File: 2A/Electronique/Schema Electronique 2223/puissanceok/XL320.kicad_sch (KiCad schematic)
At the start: 9 parts, among them J17 Conn_01x03, U4 74LVC2G241

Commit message: pcb puissance update
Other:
- moved on the sheet: C15, U4C
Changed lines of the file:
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@@
   (junction (at 156.6362 74.168) (diameter 0) (color 0 0 0 0)
   )
-  (junction (at 181.61 97.79) (diameter 0) (color 0 0 0 0)
+  (junction (at 144.018 77.724) (diameter 0) (color 0 0 0 0)
   )
   (junction (at 171.196 82.296) (diameter 0) (color 0 0 0 0)
@@
   (junction (at 163.8824 76.708) (diameter 0) (color 0 0 0 0)
   )
-  (junction (at 181.61 118.11) (diameter 0) (color 0 0 0 0)
+  (junction (at 144.018 98.044) (diameter 0) (color 0 0 0 0)
   )
   (junction (at 156.6898 74.168) (diameter 0) (color 0 0 0 0)
@@
     (stroke (width 0) (type default))
   )
-  (wire (pts (xy 189.5632 109.7211) (xy 189.5632 118.11))
+  (wire (pts (xy 151.9712 89.6551) (xy 151.9712 98.044))
     (stroke (width 0) (type default))
   )
@@
     (stroke (width 0) (type default))
   )
-  (wire (pts (xy 189.5632 97.79) (xy 189.5632 104.6411))
-    (stroke (width 0) (type default))
-  )
-  (wire (pts (xy 181.6019 97.79) (xy 181.6019 96.5499))
-    (stroke (width 0) (type default))
-  )
-  (wire (pts (xy 181.61 97.79) (xy 189.5632 97.79))
-    (stroke (width 0) (type default))
-  )
-  (wire (pts (xy 181.61 118.11) (xy 189.5632 118.11))
+  (wire (pts (xy 151.9712 77.724) (xy 151.9712 84.5751))
+    (stroke (width 0) (type default))
+  )
+  (wire (pts (xy 144.0099 77.724) (xy 144.0099 76.4839))
+    (stroke (width 0) (type default))
+  )
+  (wire (pts (xy 144.018 77.724) (xy 151.9712 77.724))
+    (stroke (width 0) (type default))
+  )
+  (wire (pts (xy 144.018 98.044) (xy 151.9712 98.044))
     (stroke (width 0) (type default))
   )
@@
     (stroke (width 0) (type default))
   )
-  (wire (pts (xy 181.6019 97.79) (xy 181.61 97.79))
+  (wire (pts (xy 144.0099 77.724) (xy 144.018 77.724))
     (stroke (width 0) (type default))
   )
@@
     (effects (font (size 1.27 1.27)) (justify right))
   )
-  (hierarchical_label "Converter_pwr" (shape input) (at 181.6019 96.5499 90) (fields_autoplaced)
+  (hierarchical_label "Converter_pwr" (shape input) (at 144.0099 76.4839 90) (fields_autoplaced)
     (effects (font (size 1.27 1.27)) (justify left))
   )
@@
     )
   )
-  (symbol (lib_id "Device:C_Small") (at 189.5632 107.1811 0) (unit 1)
-    (in_bom yes) (on_board yes) (dnp no)
-    (property "Reference" "C15" (at 190.5792 106.1651 90)
-      (effects (font (size 1.27 1.27)) (justify left))
-    )
-    (property "Value" "0.1u" (at 190.3252 109.2131 0)
-      (effects (font (size 1.27 1.27)) (justify left))
-    )
-    (property "Footprint" "" (at 189.5632 107.1811 0)
-      (effects (font (size 1.27 1.27)) hide)
-    )
-    (property "Datasheet" "~" (at 189.5632 107.1811 0)
+  (symbol (lib_id "Device:C_Small") (at 151.9712 87.1151 0) (unit 1)
+    (in_bom yes) (on_board yes) (dnp no)
+    (property "Reference" "C15" (at 152.9872 86.0991 90)
+      (effects (font (size 1.27 1.27)) (justify left))
+    )
+    (property "Value" "0.1u" (at 152.7332 89.1471 0)
+      (effects (font (size 1.27 1.27)) (justify left))
+    )
+    (property "Footprint" "" (at 151.9712 87.1151 0)
+      (effects (font (size 1.27 1.27)) hide)
+    )
+    (property "Datasheet" "~" (at 151.9712 87.1151 0)
       (effects (font (size 1.27 1.27)) hide)
     )
@@
     )
   )
-  (symbol (lib_id "power:GND") (at 181.61 118.11 0) (unit 1)
-    (in_bom yes) (on_board yes) (dnp no)
-    (property "Reference" "#PWR036" (at 181.61 124.46 0)
-      (effects (font (size 1.27 1.27)) hide)
-    )
-    (property "Value" "GND" (at 177.8 118.11 0)
+  (symbol (lib_id "power:GND") (at 144.018 98.044 0) (unit 1)
+    (in_bom yes) (on_board yes) (dnp no)
+    (property "Reference" "#PWR036" (at 144.018 104.394 0)
+      (effects (font (size 1.27 1.27)) hide)
+    )
+    (property "Value" "GND" (at 140.208 98.044 0)
       (effects (font (size 1.27 1.27)))
     )
-    (property "Footprint" "" (at 181.61 118.11 0)
-      (effects (font (size 1.27 1.27)) hide)
-    )
-    (property "Datasheet" "" (at 181.61 118.11 0)
+    (property "Footprint" "" (at 144.018 98.044 0)
+      (effects (font (size 1.27 1.27)) hide)
+    )
+    (property "Datasheet" "" (at 144.018 98.044 0)
       (effects (font (size 1.27 1.27)) hide)
     )
@@
     )
   )
-  (symbol (lib_id "74xGxx:74LVC2G241") (at 181.61 107.95 0) (unit 3)
-    (in_bom yes) (on_board yes) (dnp no)
-    (property "Reference" "U4" (at 179.07 109.728 90)
-      (effects (font (size 1.27 1.27)) (justify left))
-    )
-    (property "Value" "74LVC2G241" (at 184.658 101.854 90)
+  (symbol (lib_id "74xGxx:74LVC2G241") (at 144.018 87.884 0) (unit 3)
+    (in_bom yes) (on_board yes) (dnp no)
+    (property "Reference" "U4" (at 141.478 89.662 90)
+      (effects (font (size 1.27 1.27)) (justify left))
+    )
+    (property "Value" "74LVC2G241" (at 147.066 81.788 90)
       (effects (font (size 1.27 1.27)) (justify right))
     )
-    (property "Footprint" "" (at 181.61 107.95 0)
-      (effects (font (size 1.27 1.27)) hide)
-    )
-    (property "Datasheet" "http://www.ti.com/lit/sg/scyt129e/scyt129e.pdf" (at 181.61 107.95 0)
-      (effects (font (size 1.27 1.27)) hide)
-    )
+    (property "Footprint" "" (at 144.018 87.884 0)
+      (effects (font (size 1.27 1.27)) hide)
+    )
+    (property "Datasheet" "http://www.ti.com/lit/sg/scyt129e/scyt129e.pdf" (at 144.018 87.884 0)
+      (effects (font (size 1.27 1.27)) hide)
+    )

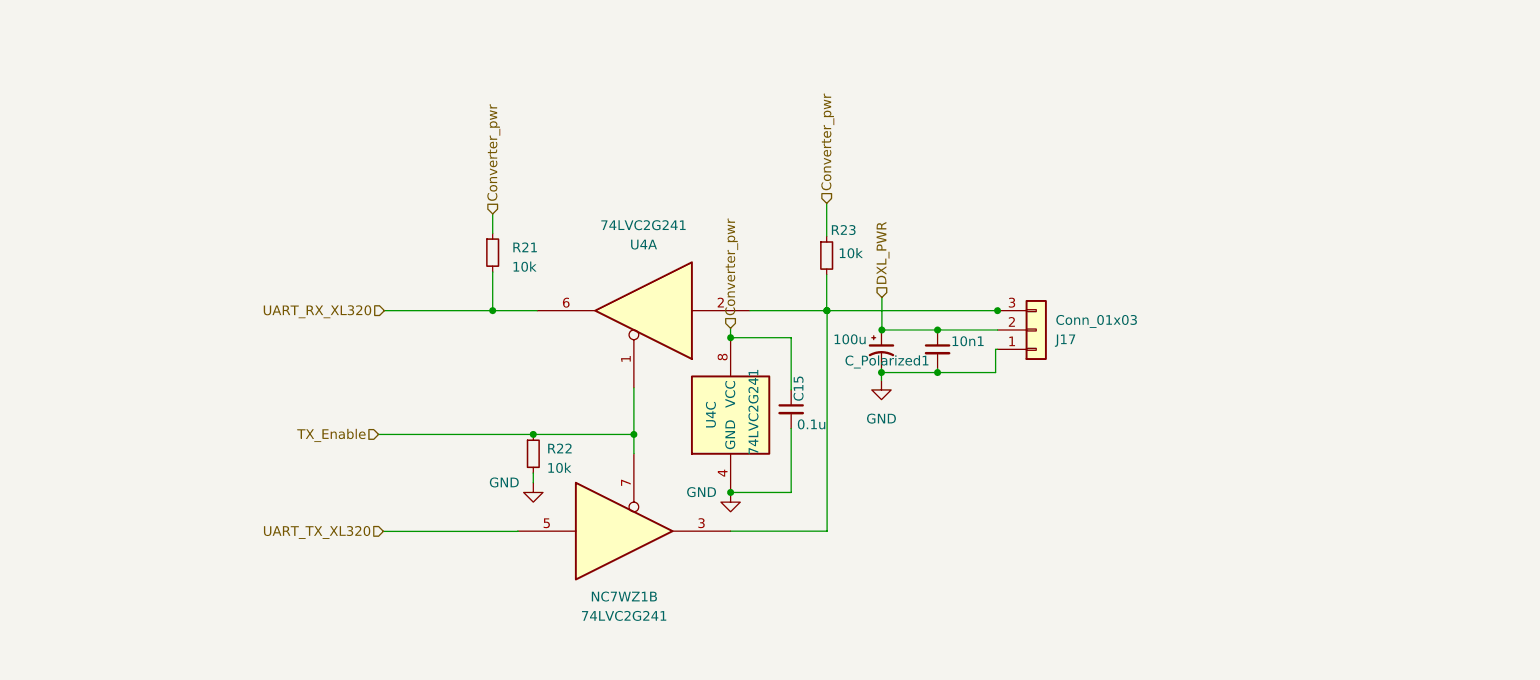
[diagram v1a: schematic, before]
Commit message: update schematic add testpoint and level shifter
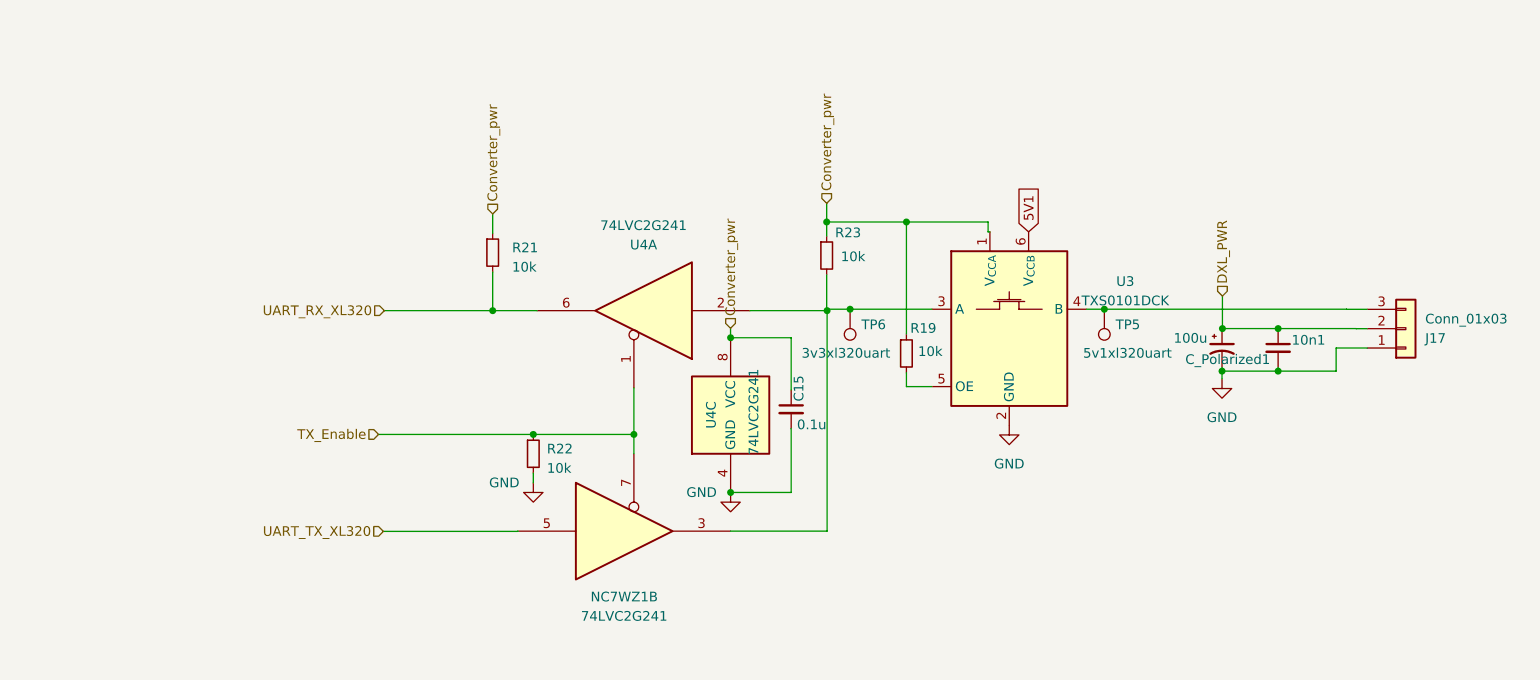
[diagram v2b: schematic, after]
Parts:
- added R19: 10k, symbol Device:R_Small
- added TP5: 5v1xl320uart, symbol Connector:TestPoint
- added TP6: 3v3xl320uart, symbol Connector:TestPoint
- added U3: TXS0101DCK, Package_TO_SOT_SMD:SOT-363_SC-70-6, symbol Logic_LevelTranslator:TXS0101DCK
- NC7WZ1: N mouser (none) -> 595-SN74LVC2G241DCTR
- U4: numero mouser (none) -> 595-SN74LVC2G241DCTR
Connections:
- net Converter_pwr: now also R19.1, U3.1 (V_{CCA})
- net GND: now also U3.2 (GND)
- net at NC7WZ1.3, U4.2: now also TP6.1, U3.3 (A); no longer J17.3 (Pin_3), R23.2
- new net: J17.3 (Pin_3), TP5.1, U3.4 (B)
- new net: R19.2, U3.5 (OE)
- new net 5V1: U3.6 (V_{CCB})
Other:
- moved on the sheet: 10n1, C_Polarized1, J17

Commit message: update schematic
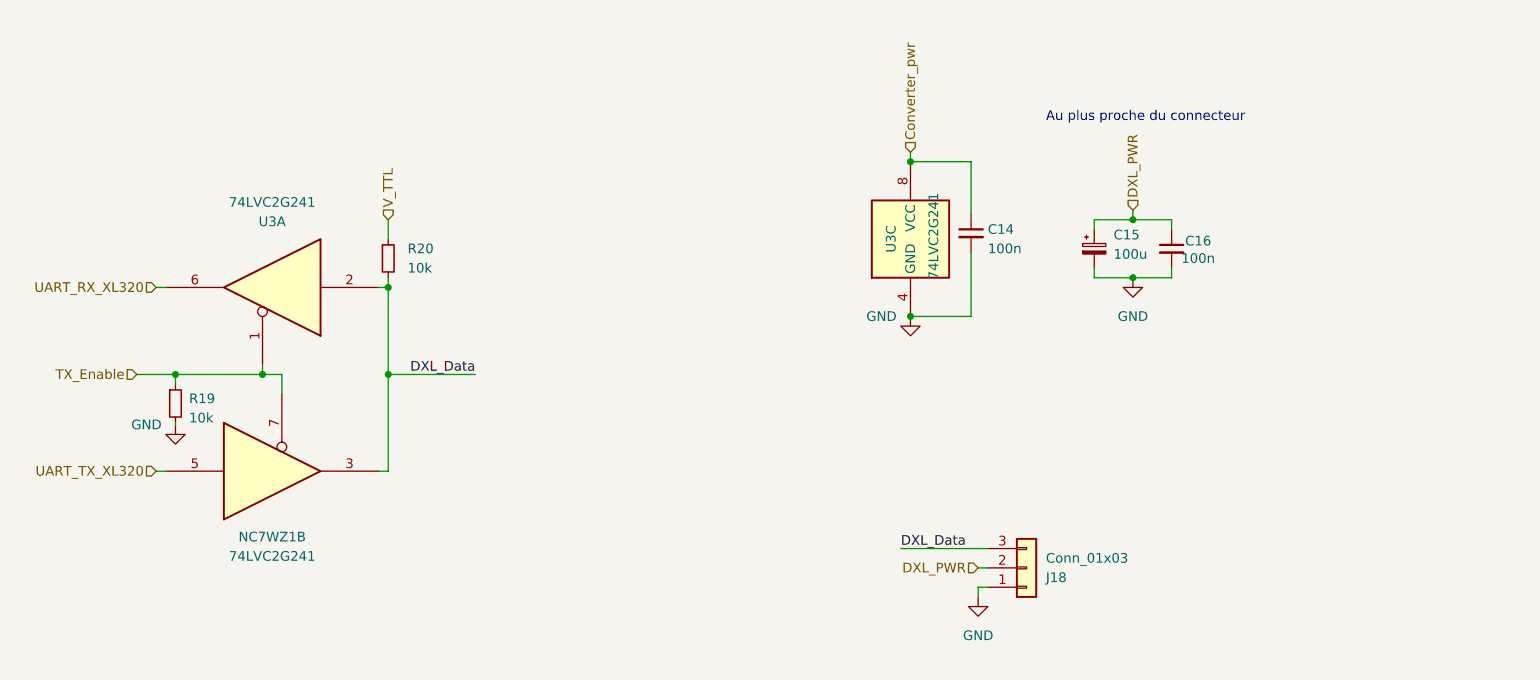
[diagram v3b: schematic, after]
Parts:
- removed 10n1: C_Small, symbol Device:C_Small
- removed C_Polarized1: 100u, symbol Device:C_Polarized_Small_US
- removed R19, R21, R23: 10k, symbol Device:R_Small
- removed TP5: 5v1xl320uart, symbol Connector:TestPoint
- removed TP6: 3v3xl320uart, symbol Connector:TestPoint
- removed U3: TXS0101DCK, Package_TO_SOT_SMD:SOT-363_SC-70-6, symbol Logic_LevelTranslator:TXS0101DCK
- added C15: 100u, symbol Device:C_Polarized_Small
- added C16: 100n, symbol Device:C_Small
- added R20: 10k, symbol Device:R_Small
- C14: renamed from C15; value 0.1u -> 100n
- renumbered J17 to J18, R22 to R19, U4 to U3
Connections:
- net DXL_PWR: now also C15.1, C16.1
- net GND: now also C15.2, C16.2
- net DXL_Data: now reaches NC7WZ1.3, U3.2
- net DXL_Data: now also J18.3 (Pin_3), R20.2
- new net V_TTL: R20.1
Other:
- note added: "Au plus proche du connecteur"
- moved on the sheet: C14, J18, NC7WZ1B, R19, U3A, U3C

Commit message: debut assignation empreintes
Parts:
- C14, C15, C16: footprint (none) -> Capacitor_SMD:C_0603_1608Metric_Pad1.08x0.95mm_HandSolder
- R19, R20: footprint (none) -> Resistor_SMD:R_0603_1608Metric_Pad0.98x0.95mm_HandSolder
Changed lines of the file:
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@@
       (effects (font (size 1.27 1.27)) (justify left))
     )
-    (property "Footprint" "" (at 201.93 66.04 0)
+    (property "Footprint" "Capacitor_SMD:C_0603_1608Metric_Pad1.08x0.95mm_HandSolder" (at 201.93 66.04 0)
       (effects (font (size 1.27 1.27)) hide)
     )
@@
       (effects (font (size 1.27 1.27)) (justify left))
     )
-    (property "Footprint" "" (at 175.5932 64.0011 0)
+    (property "Footprint" "Capacitor_SMD:C_0603_1608Metric_Pad1.08x0.95mm_HandSolder" (at 175.5932 64.0011 0)
       (effects (font (size 1.27 1.27)) hide)
     )
@@
       (effects (font (size 1.27 1.27)) (justify left))
     )
-    (property "Footprint" "" (at 71.12 86.36 0)
+    (property "Footprint" "Resistor_SMD:R_0603_1608Metric_Pad0.98x0.95mm_HandSolder" (at 71.12 86.36 0)
       (effects (font (size 1.27 1.27)) hide)
     )
@@
       (effects (font (size 1.27 1.27)) (justify left))
     )
-    (property "Footprint" "" (at 99.06 67.31 0)
+    (property "Footprint" "Resistor_SMD:R_0603_1608Metric_Pad0.98x0.95mm_HandSolder" (at 99.06 67.31 0)
       (effects (font (size 1.27 1.27)) hide)
     )
@@
       (effects (font (size 1.27 1.27)) (justify left))
     )
-    (property "Footprint" "" (at 191.77 66.04 0)
-      (effects (font (size 1.27 1.27)) hide)
-    )
+    (property "Footprint" "Capacitor_SMD:C_0603_1608Metric_Pad1.08x0.95mm_HandSolder" (at 191.77 66.04 0)
+      (effects (font (size 1.27 1.27)) hide)
+    )

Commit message: update pcd
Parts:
- removed NC7WZ1: 74LVC2G241, symbol 74xGxx:74LVC2G241
- added R19: 10k, Resistor_SMD:R_0603_1608Metric_Pad0.98x0.95mm_HandSolder, symbol Device:R_Small
- added unit 2 of U3
- C14, C16: footprint Capacitor_SMD:C_0603_1608Metric_Pad1.08x0.95mm_HandSolder -> Capacitor_SMD:C_0402_1005Metric
- C15: footprint Capacitor_SMD:C_0603_1608Metric_Pad1.08x0.95mm_HandSolder -> (none); Vmax (none) -> 10V
- J21: renamed from J18; footprint (none) -> Connector_JST:JST_XH_B3B-XH-A_1x03_P2.50mm_Vertical
- U3: numero mouser 595-SN74LVC2G241DCTR -> (none)
- renumbered R19 to R21
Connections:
- net Converter_pwr: now also R19.1
- net DXL_Data: now also U3.3
- net TX_Enable: now also U3.7
- net UART_RX_XL320: now also R19.2
- net UART_TX_XL320: now also U3.5
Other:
- note added: "3.3V Side for RPI"
- note added: "5V side for XL320"
- moved on the sheet: R20, R21

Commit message: add schematic update and footprint
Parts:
- C15: footprint (none) -> Capacitor_SMD:CP_Elec_6.3x7.7; MPN (none) -> 865060445005; Vmax 10V -> 25V
- U3: footprint (none) -> Package_SO:VSSOP-8_2.3x2mm_P0.5mm; Farnell (none) -> https://fr.farnell.com/nexperia/74lvc2g241dc-125/buffer-dri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
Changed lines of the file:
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@@
       (effects (font (size 1.27 1.27)))
     )
-    (property "Footprint" "" (at 105.41 69.85 0)
-      (effects (font (size 1.27 1.27)) hide)
-    )
-    (property "Datasheet" "http://www.ti.com/lit/sg/scyt129e/scyt129e.pdf" (at 105.41 69.85 0)
+    (property "Footprint" "Package_SO:VSSOP-8_2.3x2mm_P0.5mm" (at 105.41 69.85 0)
+      (effects (font (size 1.27 1.27)) hide)
+    )
+    (property "Datasheet" "https://4donline.ihs.com/images/VipMasterIC/IC/PHGL/PHGLS27073/PHGLS27073-1.pdf?hkey=6D3A4C79FDBF58556ACFDE234799DDF0" (at 105.41 69.85 0)
+      (effects (font (size 1.27 1.27)) hide)
+    )
+    (property "Farnell" "https://fr.farnell.com/nexperia/74lvc2g241dc-125/buffer-driver-de-ligne-40-a-125/dp/3442085?st=74LVC2G241DC,125" (at 105.41 69.85 0)
       (effects (font (size 1.27 1.27)) hide)
     )
@@
       (effects (font (size 1.27 1.27)))
     )
-    (property "Footprint" "" (at 107.95 93.98 0)
-      (effects (font (size 1.27 1.27)) hide)
-    )
-    (property "Datasheet" "http://www.ti.com/lit/sg/scyt129e/scyt129e.pdf" (at 107.95 93.98 0)
+    (property "Footprint" "Package_SO:VSSOP-8_2.3x2mm_P0.5mm" (at 107.95 93.98 0)
+      (effects (font (size 1.27 1.27)) hide)
+    )
+    (property "Datasheet" "https://4donline.ihs.com/images/VipMasterIC/IC/PHGL/PHGLS27073/PHGLS27073-1.pdf?hkey=6D3A4C79FDBF58556ACFDE234799DDF0" (at 107.95 93.98 0)
+      (effects (font (size 1.27 1.27)) hide)
+    )
+    (property "Farnell" "https://fr.farnell.com/nexperia/74lvc2g241dc-125/buffer-driver-de-ligne-40-a-125/dp/3442085?st=74LVC2G241DC,125" (at 107.95 93.98 0)
       (effects (font (size 1.27 1.27)) hide)
     )
@@
       (effects (font (size 1.27 1.27)) (justify left))
     )
-    (property "Footprint" "" (at 167.64 64.77 0)
-      (effects (font (size 1.27 1.27)) hide)
-    )
-    (property "Datasheet" "http://www.ti.com/lit/sg/scyt129e/scyt129e.pdf" (at 167.64 64.77 0)
+    (property "Footprint" "Package_SO:VSSOP-8_2.3x2mm_P0.5mm" (at 167.64 64.77 0)
+      (effects (font (size 1.27 1.27)) hide)
+    )
+    (property "Datasheet" "https://4donline.ihs.com/images/VipMasterIC/IC/PHGL/PHGLS27073/PHGLS27073-1.pdf?hkey=6D3A4C79FDBF58556ACFDE234799DDF0" (at 167.64 64.77 0)
+      (effects (font (size 1.27 1.27)) hide)
+    )
+    (property "Farnell" "https://fr.farnell.com/nexperia/74lvc2g241dc-125/buffer-driver-de-ligne-40-a-125/dp/3442085?st=74LVC2G241DC,125" (at 167.64 64.77 0)
       (effects (font (size 1.27 1.27)) hide)
     )
@@
       (effects (font (size 1.27 1.27)) (justify left))
     )
-    (property "Footprint" "" (at 191.77 66.04 0)
+    (property "Footprint" "Capacitor_SMD:CP_Elec_6.3x7.7" (at 191.77 66.04 0)
       (effects (font (size 1.27 1.27)) hide)
     )
@@
       (effects (font (size 1.27 1.27)) hide)
     )
-    (property "Vmax" "10V" (at 191.77 66.04 0)
-      (effects (font (size 1.27 1.27)) hide)
-    )
-    (property "MPN" "" (at 191.77 66.04 0)
-      (effects (font (size 1.27 1.27)) hide)
-    )
+    (property "Vmax" "25V" (at 191.77 66.04 0)
+      (effects (font (size 1.27 1.27)) hide)
+    )
+    (property "MPN" "865060445005" (at 191.77 66.04 0)
+      (effects (font (size 1.27 1.27)) hide)
+    )

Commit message: finalize schematic + footprints
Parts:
- J21: value Conn_01x03 -> Conn_XL320
- R19, R20, R21: footprint Resistor_SMD:R_0603_1608Metric_Pad0.98x0.95mm_HandSolder -> Resistor_SMD:R_0402_1005Metric
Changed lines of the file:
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@@
       (effects (font (size 1.27 1.27)) (justify left))
     )
-    (property "Value" "Conn_01x03" (at 185.42 106.68 0)
+    (property "Value" "Conn_XL320" (at 185.42 106.68 0)
       (effects (font (size 1.27 1.27)) (justify left))
     )
@@
       (effects (font (size 1.27 1.27)) (justify left))
     )
-    (property "Footprint" "Resistor_SMD:R_0603_1608Metric_Pad0.98x0.95mm_HandSolder" (at 87.63 64.77 0)
+    (property "Footprint" "Resistor_SMD:R_0402_1005Metric" (at 87.63 64.77 0)
       (effects (font (size 1.27 1.27)) hide)
     )
@@
       (effects (font (size 1.27 1.27)) (justify left))
     )
-    (property "Footprint" "Resistor_SMD:R_0603_1608Metric_Pad0.98x0.95mm_HandSolder" (at 93.98 85.09 0)
+    (property "Footprint" "Resistor_SMD:R_0402_1005Metric" (at 93.98 85.09 0)
       (effects (font (size 1.27 1.27)) hide)
     )
@@
       (effects (font (size 1.27 1.27)) (justify left))
     )
-    (property "Footprint" "Resistor_SMD:R_0603_1608Metric_Pad0.98x0.95mm_HandSolder" (at 121.92 66.04 0)
-      (effects (font (size 1.27 1.27)) hide)
-    )
+    (property "Footprint" "Resistor_SMD:R_0402_1005Metric" (at 121.92 66.04 0)
+      (effects (font (size 1.27 1.27)) hide)
+    )
